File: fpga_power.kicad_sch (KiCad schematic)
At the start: 52 parts, among them U10 AP62200TWU-7, U11 AP62200TWU-7, U12 AP62200TWU-7, U2 XC7A50T-FGG484, U9 AP62200TWU-7

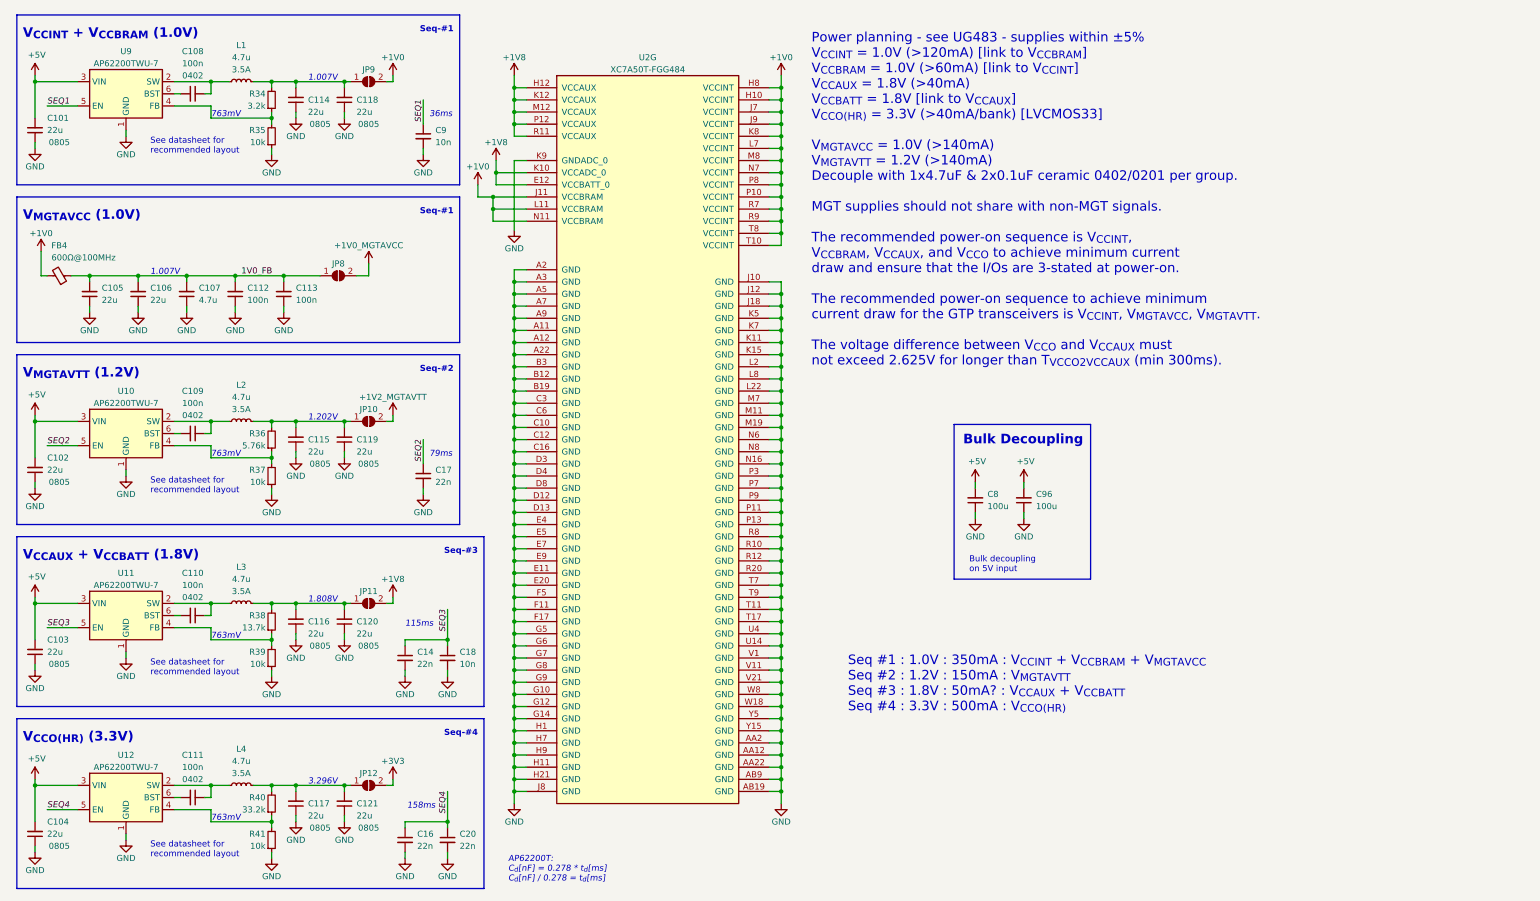
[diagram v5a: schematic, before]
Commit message: Updated decoupling. Need to work out larger planes and fills.
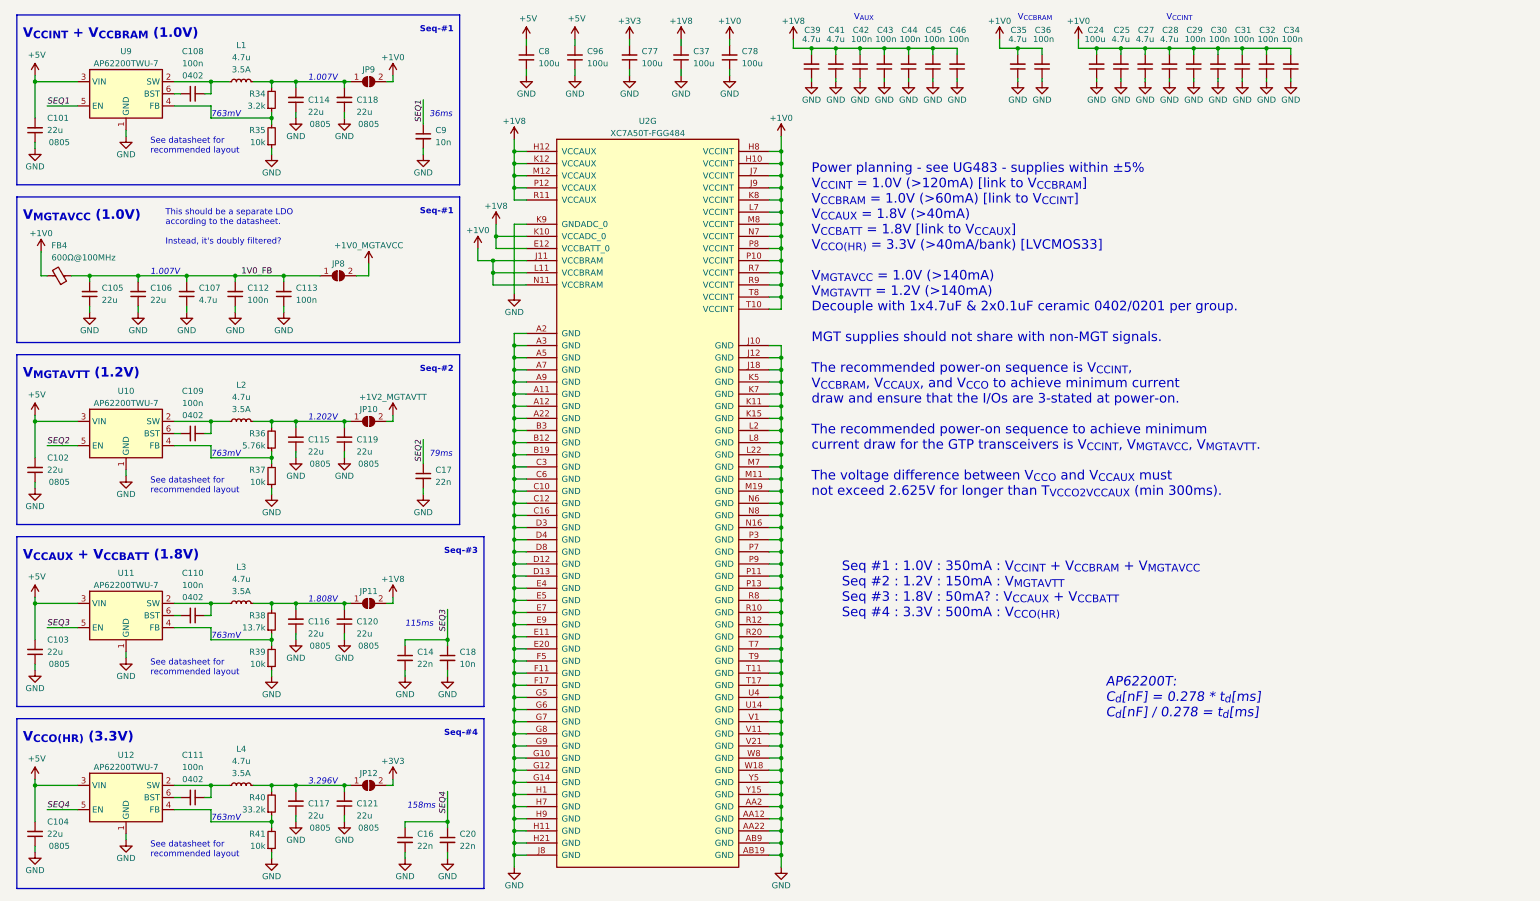
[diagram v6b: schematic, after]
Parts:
- added C24, C37, C77, C78: 100u, Capacitor_SMD:C_1206_3216Metric_Pad1.33x1.80mm_HandSolder, symbol Device:C_Small
- added C25, C27, C28, C35, C39, C41: 4.7u, Capacitor_SMD:C_0402_1005Metric_Pad0.74x0.62mm_HandSolder, symbol Device:C_Small
- added C29, C30, C31, C32, C34, C36, C42, C43, C44, C45, C46: 100n, Capacitor_SMD:C_0402_1005Metric_Pad0.74x0.62mm_HandSolder, symbol Device:C_Small
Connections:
- net +1V0: now also C24.2, C25.2, C27.2, C28.2, C29.2, C30.2, C31.2, C32.2, C34.2, C35.2, C36.2, C78.2
- net +1V8: now also C37.2, C39.2, C41.2, C42.2, C43.2, C44.2, C45.2, C46.2
- net +3V3: now also C77.2
- net GND: now also C24.1, C25.1, C27.1, C28.1, C29.1, C30.1, C31.1, C32.1, C34.1, C35.1, C36.1, C37.1, C39.1, C41.1, C42.1, C43.1, C44.1, C45.1, C46.1, C77.1, C78.1
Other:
- note added: "This should be a separate LDO according to the datasheet. Instead, it's doubly filtered?"
- note added: "V_{AUX}"
- note added: "V_{CCBRAM}"
- note added: "V_{CCINT}"
- note removed: "Bulk Decoupling"
- note removed: "Bulk decoupling on 5V input"
- title: FPGA Power Supplies & Sequencing -> FPGA Power Supplies & Core Decoupling
- moved on the sheet: C8, C96, U2G

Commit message: Routing finished; Need to battle through the DRCs now. There's a few!
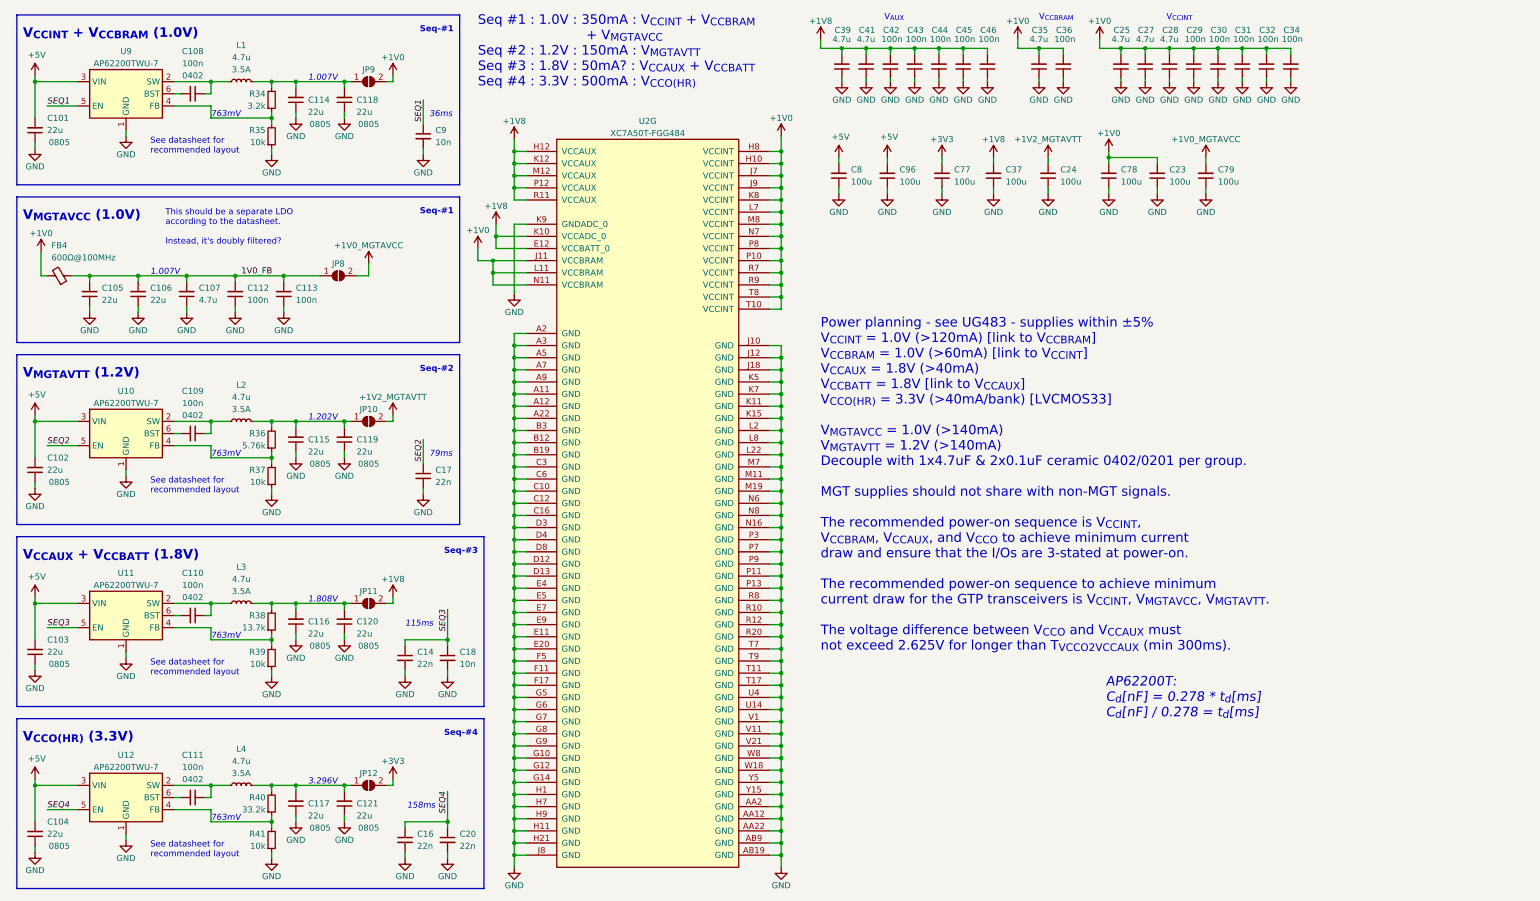
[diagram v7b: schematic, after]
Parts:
- added C23, C79: 100u, Capacitor_SMD:C_1206_3216Metric_Pad1.33x1.80mm_HandSolder, symbol Device:C_Small
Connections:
- net +1V0: now also C23.2; no longer C24.2
- net +1V0_MGTAVCC: now also C79.2
- net +1V2_MGTAVTT: now also C24.2
- net GND: now also C23.1, C79.1
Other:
- moved on the sheet: C35, C36, C37, C39, C41, C42, C43, C44, C45, C46, C77, C78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

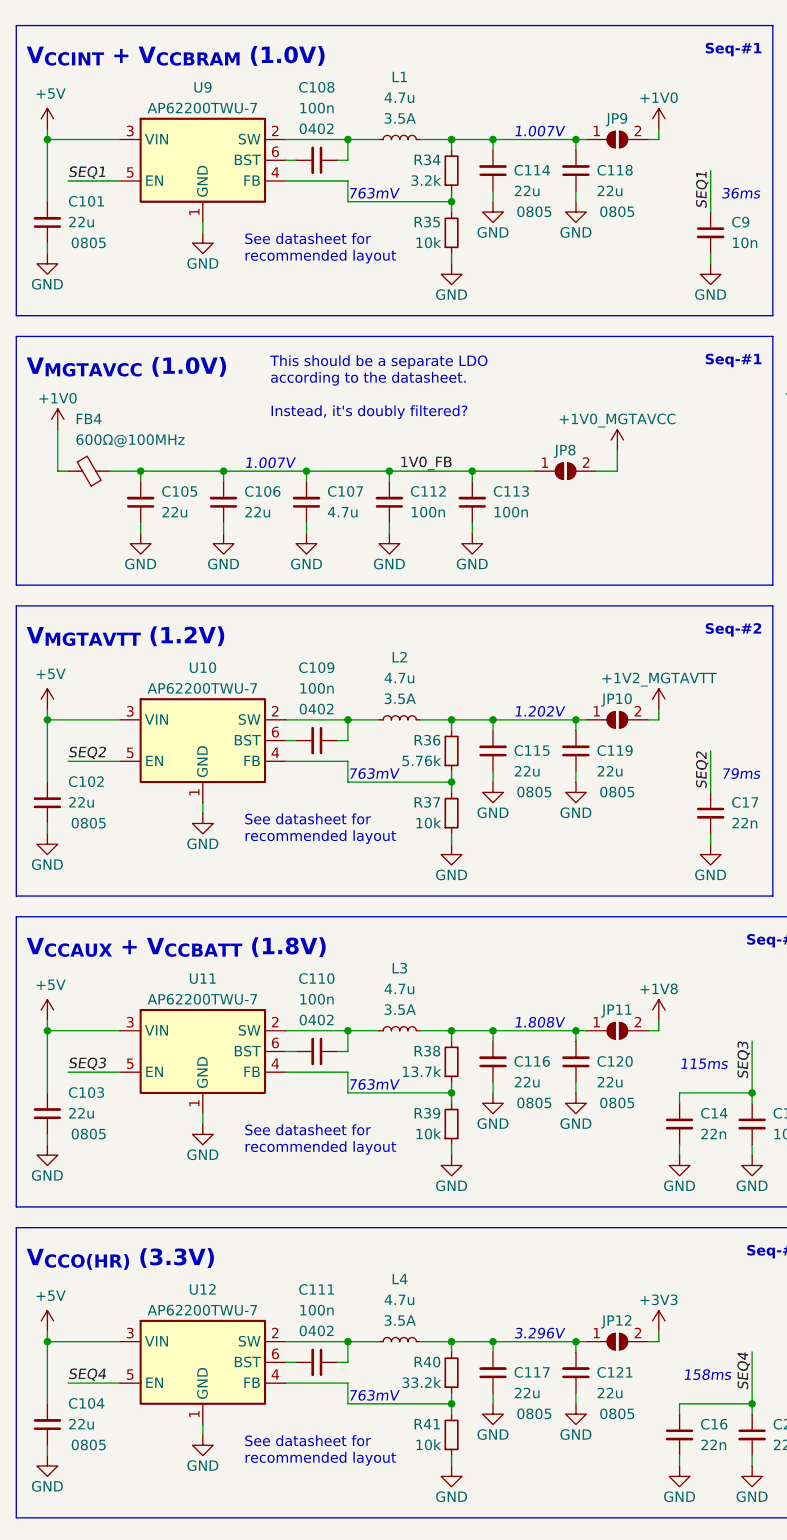
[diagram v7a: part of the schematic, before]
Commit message: Ordered boards from JLCPCB for V1
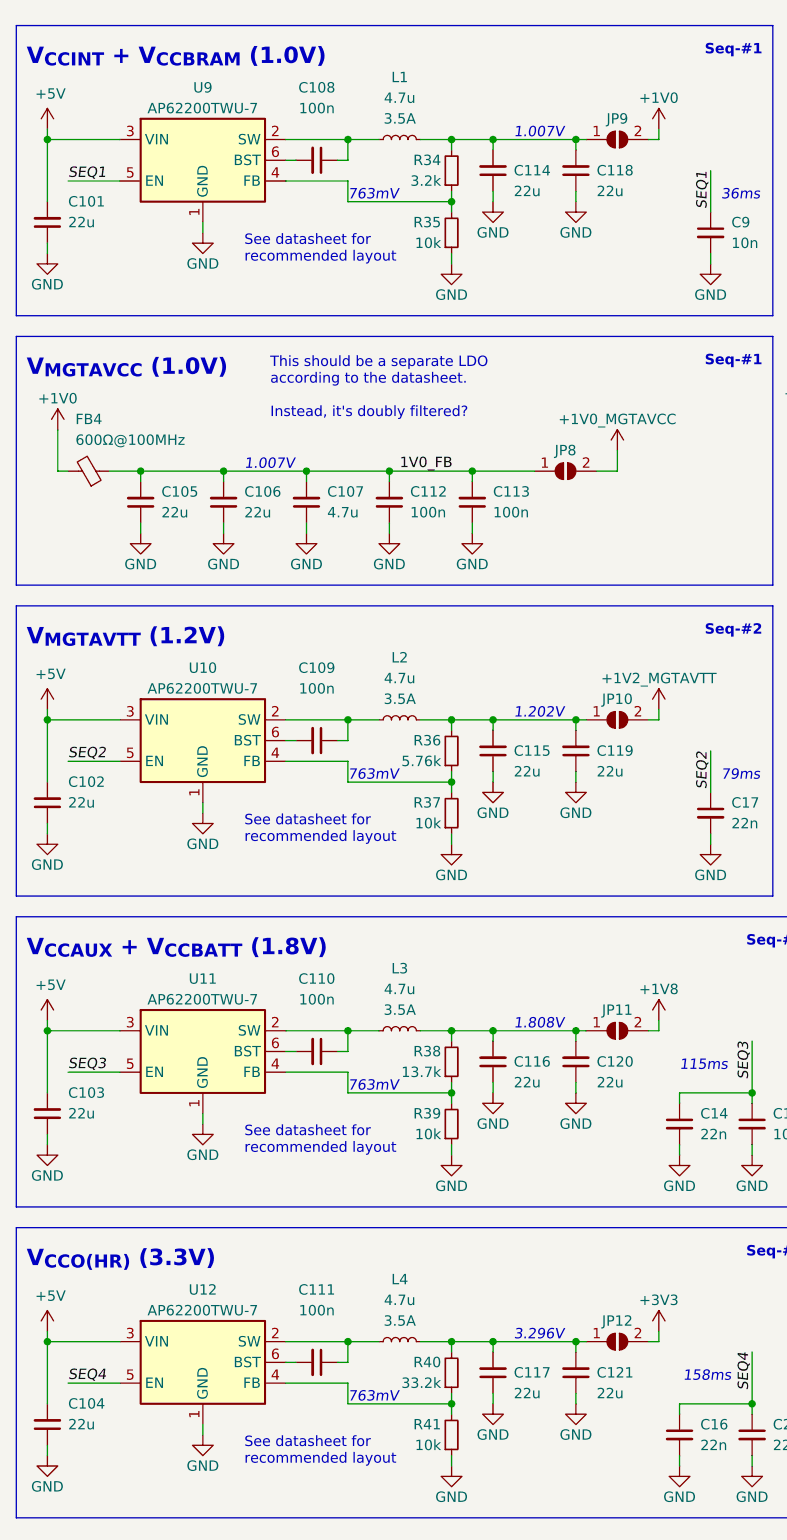
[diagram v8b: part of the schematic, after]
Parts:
- C101, C102, C103, C104, C105, C106, C114, C115, C116, C117, C118, C119, C120, C121: Pkg 0805 -> (none)
- C107, C112, C113, C25, C27, C28, C29, C30, C31, C32, C34, C35, C36, C39, C41, C42, C43, C44, C45, C46: footprint Capacitor_SMD:C_0402_1005Metric_Pad0.74x0.62mm_HandSolder -> Capacitor_SMD:C_0402_1005Metric
- C108, C109, C110, C111, C14, C16, C17, C18, C20, C9: Pkg 0402 -> (none)
- C23, C24, C37, C77, C78, C79, C8, C96: footprint Capacitor_SMD:C_1206_3216Metric_Pad1.33x1.80mm_HandSolder -> Capacitor_SMD:C_1206_3216Metric
- FB4: footprint Inductor_SMD:L_0603_1608Metric_Pad1.05x0.95mm_HandSolder -> Inductor_SMD:L_0603_1608Metric
- JP10, JP11, JP12, JP8, JP9: value ID_WP -> JUMPER; LCSC (none) -> C17888
- U10, U11, U12, U9: LCSC (none) -> C2895288
